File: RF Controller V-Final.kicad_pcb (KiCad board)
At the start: 2 copper layers, 36 parts, among them J2 J_OLED, J3 BAT+, J4 BAT-, SW1 EG1218, U1 Teensy4.0, U3 NRF24L01, U5 AP2112K-3.3, U7 Pitch/Roll, U8 TPS542025DDCR, U9 Throttle/Yaw

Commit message: Board outline
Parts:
- added C2: 47uF, 865080543009:WCAP-ASLI_6.3X5.5_DXL_, F.Cu at (90.8, 108.5)
- C7: value 22u -> 10u
- moved L1 66.1 mm to (56.9, 112.1)
- moved H4 63.0 mm to (115.5, 169.5)
- moved H3 55.9 mm to (127.0, 155.5)
- moved H2 53.5 mm to (112.5, 150.5)
- moved U5 43.5 mm to (56.0, 123.1)
- moved H1 38.2 mm to (117.0, 130.0)
- moved D6 38.2 mm to (89.6, 121.5)
- moved J4 38.2 mm to (91.7, 116.0)
- moved J3 38.2 mm to (87.6, 116.0)
- moved U8 38.0 mm to (56.9, 118.5)
- moved C1 35.2 mm to (67.6, 100.3)
- moved C10 35.2 mm to (67.6, 109.4)
- moved C13 35.2 mm to (67.6, 112.4)
- moved C14 35.2 mm to (67.6, 115.4)
- moved C15 35.2 mm to (67.6, 118.4)
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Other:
- board outline added: 131.9 x 67.5 mm

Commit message: Fixed board measurements
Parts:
- moved H2 172.0 mm to (256.5, 56.5)
- moved H4 150.8 mm to (256.5, 116.0)
- moved H1 75.3 mm to (133.5, 56.5)
- moved H3 40.0 mm to (133.5, 116.0)
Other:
- board size 131.9 x 67.5 mm -> 132 x 67.5 mm
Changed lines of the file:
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@@
 	(footprint "RF_MountingHoles:MountingHole_3.8mm"
 		(layer "F.Cu")
-		(at 112.5 150.5)
+		(at 256.5 56.5)
 		(descr "Non-plated mounting hole, 3.8 mm drill; replaces original Edge.Cuts circle")
 		(tags "mounting hole NPTH 3.8mm")
@@
 	(footprint "RF_MountingHoles:MountingHole_3.8mm"
 		(layer "F.Cu")
-		(at 117 130)
+		(at 133.5 56.5)
 		(descr "Non-plated mounting hole, 3.8 mm drill; replaces original Edge.Cuts circle")
 		(tags "mounting hole NPTH 3.8mm")
@@
 	(footprint "RF_MountingHoles:MountingHole_3.8mm"
 		(layer "F.Cu")
-		(at 115.5 169.5)
+		(at 256.5 116)
 		(descr "Non-plated mounting hole, 3.8 mm drill; replaces original Edge.Cuts circle")
 		(tags "mounting hole NPTH 3.8mm")
@@
 	(footprint "RF_MountingHoles:MountingHole_3.8mm"
 		(layer "F.Cu")
-		(at 127 155.5)
+		(at 133.5 116)
 		(descr "Non-plated mounting hole, 3.8 mm drill; replaces original Edge.Cuts circle")
 		(tags "mounting hole NPTH 3.8mm")
@@
 	)
 	(gr_line
-		(start 132 55.5)
-		(end 132 117)
+		(start 129 55.5)
+		(end 129 117)
 		(stroke
 			(width 0.1)
@@
 	)
 	(gr_arc
-		(start 132 55.5)
-		(mid 132.87868 53.37868)
-		(end 135 52.5)
+		(start 129 55.5)
+		(mid 129.87868 53.37868)
+		(end 132 52.5)
 		(stroke
 			(width 0.1)
-			(type solid)
+			(type default)
 		)
 		(layer "Edge.Cuts")
 	)
 	(gr_line
-		(start 135 52.5)
-		(end 261 52.5)
+		(start 132 52.5)
+		(end 258 52.5)
 		(stroke
 			(width 0.1)
@@
 	)
 	(gr_arc
-		(start 135 120)
-		(mid 132.878681 119.12132)
-		(end 132 117)
+		(start 132 120)
+		(mid 129.87868 119.12132)
+		(end 129 117)
 		(stroke
 			(width 0.1)
-			(type solid)
+			(type default)
 		)
 		(layer "Edge.Cuts")
 	)
 	(gr_line
-		(start 135 120)
-		(end 260.878678 120)
+		(start 132 120)
+		(end 258 120)
 		(stroke
-			(width 0.05)
-			(type default)
+			(width 0.1)
+			(type solid)
 		)
 		(layer "Edge.Cuts")
 	)
 	(gr_arc
-		(start 261 52.5)
-		(mid 263.044203 53.420281)
-		(end 263.87868 55.5)
+		(start 258 52.5)
+		(mid 260.12132 53.37868)
+		(end 261 55.5)
 		(stroke
 			(width 0.1)
@@
 	)
 	(gr_line
-		(start 263.87868 55.5)
-		(end 263.87868 117)
+		(start 261 55.5)
+		(end 261 117)
 		(stroke
 			(width 0.1)
@@
 	)
 	(gr_arc
-		(start 263.87868 117)
-		(mid 262.999999 119.121321)
-		(end 260.878678 120)
+		(start 261 117)
+		(mid 260.12132 119.12132)
+		(end 258 120)
 		(stroke
 			(width 0.1)
-			(type solid)
+			(type default)
 		)
 		(layer "Edge.Cuts")
 	)
+	(dimension
+		(type orthogonal)
+		(layer "Edge.Cuts")
+		(pts
+			(xy 132 52.5) (xy 258 52.5)
+		)
+		(height -4)
+		(orientation 0)
+		(format
+			(prefix "")
+			(suffix "")
+			(units 3)
+			(units_format 0)
+			(precision 4)
+			(suppress_zeroes yes)
+		)
+		(style
+			(thickness 0.05)
+			(arrow_length 1.27)
+			(text_position_mode 0)
+			(arrow_direction outward)
+			(extension_height 0.58642)
+			(extension_offset 0.5)
+			(keep_text_aligned yes)
+		)
+		(gr_text "126"
+			(at 195 47.35 0)
+			(layer "Edge.Cuts")
+			(effects
+				(font
+					(size 1 1)
+					(thickness 0.15)
+				)
+			)
+		)
+	)
+	(dimension
+		(type orthogonal)
+		(layer "Edge.Cuts")
+		(pts
+			(xy 258 52.5) (xy 258 55.5)
+		)
+		(height 5.5)
+		(orientation 1)
+		(format
+			(prefix "")
+			(suffix "")
+			(units 3)
+			(units_format 0)
+			(precision 4)
+			(suppress_zeroes yes)
+		)
+		(style
+			(thickness 0.05)
+			(arrow_length 1.27)
+			(text_position_mode 0)
+			(arrow_direction outward)
+			(extension_height 0.58642)
+			(extension_offset 0.5)
+			(keep_text_aligned yes)
+		)
+		(gr_text "3"
+			(at 262.35 54 90)
+			(layer "Edge.Cuts")
+			(effects
+				(font
+					(size 1 1)
+					(thickness 0.15)
+				)
+			)
+		)
+	)
+	(dimension
+		(type orthogonal)
+		(layer "Edge.Cuts")
+		(pts
+			(xy 261 55.5) (xy 261 117)
+		)
+		(height 4)
+		(orientation 1)
+		(format
+			(prefix "")
+			(suffix "")
+			(units 3)
+			(units_format 0)
+			(precision 4)
+			(suppress_zeroes yes)
+		)
+		(style
+			(thickness 0.05)
+			(arrow_length 1.27)
+			(text_position_mode 0)
+			(arrow_direction outward)
+			(extension_height 0.58642)
+			(extension_offset 0.5)
+			(keep_text_aligned yes)
+		)
+		(gr_text "61.5"
+			(at 263.85 86.25 90)
+			(layer "Edge.Cuts")
+			(effects
+				(font
+					(size 1 1)
+					(thickness 0.15)
+				)
+			)
+		)
+	)
 	(embedded_fonts no)

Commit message: Placed some components
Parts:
- ?: renamed from U1; value Teensy4.0 -> (none)
- moved U7 183.1 mm to (210.0, 115.5)
- moved J2 160.2 mm to (235.5, 58.3)
- moved U9 150.7 mm to (180.0, 89.5), turned to 180 degrees
- moved U3 138.7 mm to (206.4, 62.0), turned to 90 degrees
- moved ? 121.6 mm to (148.6, 74.0)
- moved D6 95.6 mm to (161.0, 58.0), turned to 180 degrees
- moved C2 91.4 mm to (174.0, 70.5)
- moved SW1 76.1 mm to (148.5, 58.0)

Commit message: Component layout V1
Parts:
- removed ?: , teensy:Teensy40
- added U1: Teensy4.0, teensy:Teensy40, F.Cu at (101.5, 93.5)
- C11: value 22u -> 10u
- C12: value 10u -> 22u
- D7: value APT2012LZGCK -> (none)
- SW1: value EG1218 -> (none)
- U5: value AP2112K-3.3 -> (none)
- U8: value TPS542025DDCR -> (none)
- moved C1 109.6 mm to (175.5, 81.5)
- moved R2 107.6 mm to (175.5, 72.5), turned to 180 degrees
- moved R1 105.9 mm to (175.5, 76.5)
- moved U5 96.2 mm to (138.5, 73.5)
- moved C6 81.0 mm to (145.0, 79.5)
- moved C14 80.4 mm to (139.0, 78.5), turned to 180 degrees
- moved C5 78.7 mm to (145.0, 71.0)
- moved C11 78.6 mm to (145.0, 74.5)
- moved L1 78.3 mm to (125.0, 73.5)
- moved U8 75.5 mm to (116.0, 71.5)
- moved C15 75.5 mm to (131.0, 77.5), turned to 180 degrees
- moved C12 65.5 mm to (132.0, 72.0), turned to 90 degrees
- moved R7 62.1 mm to (119.5, 77.5), turned to 90 degrees
- moved R6 57.5 mm to (115.0, 76.5), turned to 180 degrees
- moved D6 55.4 mm to (107.5, 72.5)
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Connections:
- net Net-(U8-SW) renamed /BUCK_SW
- C11 pad 1: /5V_IN -> /3.3V_OUT
- C12 pad 1: /3.3V_OUT -> /5V_IN
- SW1 pad 1: unconnected-(SW1-A-Pad1) -> /VBAT
- SW1 pad 3: /VBAT -> unconnected-(SW1-C-Pad3)

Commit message: PCB Wiring V1
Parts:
- turned R3 to 180 degrees
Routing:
- net /3.3V_OUT: track 0.00 -> 151.6 mm
- net GND: track 0.00 -> 98.5 mm, vias 0 -> 19
- net /9V_IN: track 0.00 -> 23.7 mm, vias 0 -> 5
- net Net-(U8-BOOT): track 0.00 -> 15.9 mm
- net /ADC7: track 0.00 -> 14.7 mm
- net /SW_OUT: track 0.00 -> 14.2 mm
- net Net-(U8-EN): track 0.00 -> 10.3 mm, vias 0 -> 4
- net /VBAT: track 0.00 -> 8.74 mm
- net /BUCK_SW: track 0.00 -> 8.61 mm
- net /ADC6: track 0.00 -> 7.66 mm, vias 0 -> 4
- net Net-(D7-A): track 0.00 -> 3.18 mm
- added copper zone on F.Cu, net /5V_IN
- added copper zone on B.Cu, net GND

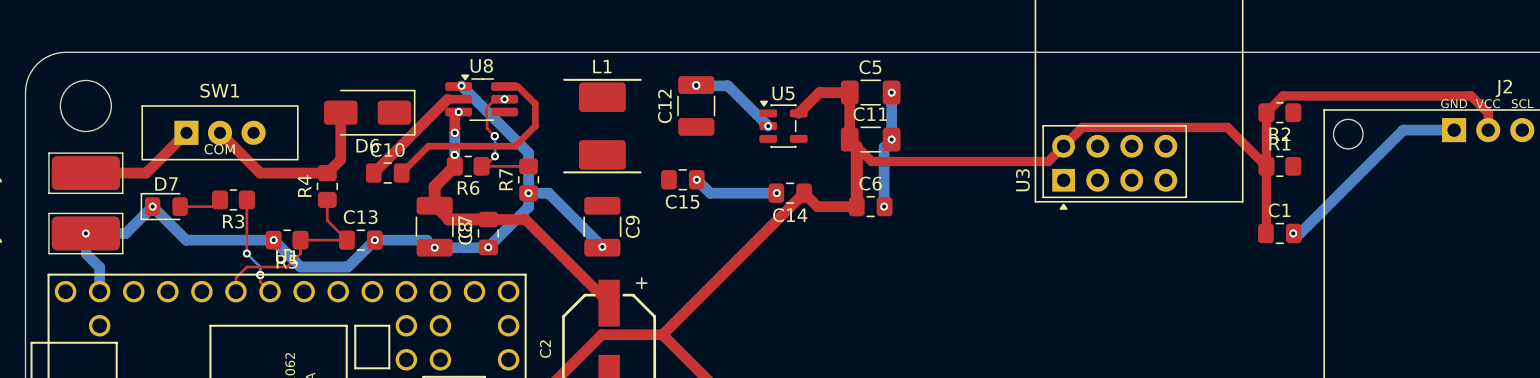
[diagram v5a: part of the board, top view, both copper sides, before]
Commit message: Replaced ground wires with vias at nodes
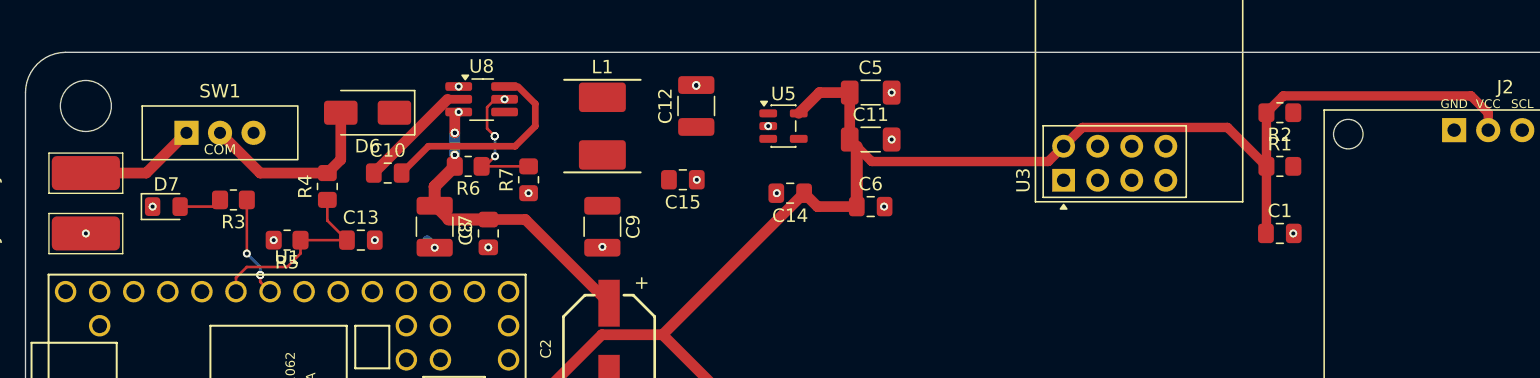
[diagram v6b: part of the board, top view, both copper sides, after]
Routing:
- net GND: track 98.5 -> 1.34 mm, vias 19 -> 18
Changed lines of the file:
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@@
-	)
-	(via
-		(at 87.53 85.84)
-		(size 0.6)
-		(drill 0.3)
-		(layers "F.Cu" "B.Cu")
-		(net "GND")
 	)
 	(via
@@
 	)
 	(via
+		(at 114.29 70.55)
+		(size 0.6)
+		(drill 0.3)
+		(layers "F.Cu" "B.Cu")
+		(net "GND")
+	)
+	(via
 		(at 116.5 82.5375)
 		(size 0.6)
@@
 	(via
 		(at 91.475 79.5)
-		(size 0.6)
-		(drill 0.3)
-		(layers "F.Cu" "B.Cu")
-		(net "GND")
-	)
-	(via
-		(at 114.5 70.5)
 		(size 0.6)
 		(drill 0.3)
@@
 	)
 	(segment
-		(start 86.5 81.5)
-		(end 86.5 83)
-		(width 0.7)
-		(layer "B.Cu")
-		(net "GND")
-	)
-	(segment
-		(start 132 70.5)
-		(end 134.3625 70.5)
-		(width 0.8)
-		(layer "B.Cu")
-		(net "GND")
-	)
-	(segment
-		(start 133.0375 78.5)
-		(end 132.0375 77.5)
-		(width 0.8)
-		(layer "B.Cu")
-		(net "GND")
-	)
-	(segment
-		(start 146.5625 74.5)
-		(end 146.5625 71)
-		(width 0.8)
-		(layer "B.Cu")
-		(net "GND")
-	)
-	(segment
-		(start 106.0375 84)
-		(end 108.0375 82)
-		(width 0.8)
-		(layer "B.Cu")
-		(net "GND")
-	)
-	(segment
-		(start 184.7 73.8)
-		(end 188.49 73.8)
-		(width 0.8)
-		(layer "B.Cu")
-		(net "GND")
-	)
-	(segment
-		(start 121 78.5)
-		(end 119.5 78.5)
-		(width 0.8)
-		(layer "B.Cu")
-		(net "GND")
-	)
-	(segment
-		(start 134.3625 70.5)
-		(end 137.3625 73.5)
-		(width 0.8)
-		(layer "B.Cu")
-		(net "GND")
-	)
-	(segment
-		(start 146 75.0625)
-		(end 146.5625 74.5)
-		(width 0.7)
-		(layer "B.Cu")
-		(net "GND")
-	)
-	(segment
-		(start 86.5 81.5)
-		(end 89.475 81.5)
-		(width 0.8)
-		(layer "B.Cu")
-		(net "GND")
-	)
-	(segment
-		(start 100.5 82)
-		(end 102.5 84)
-		(width 0.8)
-		(layer "B.Cu")
-		(net "GND")
-	)
-	(segment
-		(start 86.5 83)
-		(end 87.53 84.03)
-		(width 0.8)
-		(layer "B.Cu")
-		(net "GND")
-	)
-	(segment
-		(start 146 79.5)
-		(end 146 75.0625)
-		(width 0.8)
-		(layer "B.Cu")
-		(net "GND")
-	)
-	(segment
-		(start 87.53 84.03)
-		(end 87.53 85.84)
-		(width 0.8)
-		(layer "B.Cu")
-		(net "GND")
-	)
-	(segment
-		(start 102.5 84)
-		(end 106.0375 84)
-		(width 0.8)
-		(layer "B.Cu")
-		(net "GND")
-	)
-	(segment
-		(start 119.5 75.5)
-		(end 119.5 78.5)
-		(width 0.8)
-		(layer "B.Cu")
-		(net "GND")
-	)
-	(segment
-		(start 119.5 79.5375)
-		(end 116.475 82.5625)
-		(width 0.8)
-		(layer "B.Cu")
-		(net "GND")
-	)
-	(segment
-		(start 138 78.5)
-		(end 133.0375 78.5)
-		(width 0.8)
-		(layer "B.Cu")
-		(net "GND")
-	)
-	(segment
-		(start 177 81.5)
-		(end 184.7 73.8)
-		(width 0.8)
-		(layer "B.Cu")
-		(net "GND")
-	)
-	(segment
-		(start 89.475 81.5)
-		(end 91.475 79.5)
-		(width 0.8)
-		(layer "B.Cu")
-		(net "GND")
-	)
-	(segment
-		(start 112.5 82.5625)
-		(end 116.475 82.5625)
-		(width 0.8)
-		(layer "B.Cu")
-		(net "GND")
-	)
-	(segment
 		(start 111.9375 82)
 		(end 112.5 82.5625)
@@
 		(layer "B.Cu")
 		(net "GND")
-	)
-	(segment
-		(start 176.5 81.5)
-		(end 177 81.5)
-		(width 0.8)
-		(layer "B.Cu")
-		(net "GND")
-	)
-	(segment
-		(start 91.475 79.5)
-		(end 93.975 82)
-		(width 0.8)
-		(layer "B.Cu")
-		(net "GND")
-	)
-	(segment
-		(start 119.5 78.5)
-		(end 119.5 79.5375)
-		(width 0.8)
-		(layer "B.Cu")
-		(net "GND")
-	)
-	(segment
-		(start 114.5 70.5)
-		(end 119.5 75.5)
-		(width 0.8)
-		(layer "B.Cu")
-		(net "GND")
-	)
-	(segment
-		(start 93.975 82)
-		(end 100.5 82)
-		(width 0.8)
-		(layer "B.Cu")
-		(net "GND")
-	)
-	(segment
-		(start 108.0375 82)
-		(end 111.9375 82)
-		(width 0.8)
-		(layer "B.Cu")
-		(net "GND")
-	)
-	(segment
-		(start 125 82.5)
-		(end 121 78.5)
-		(width 0.8)
-		(layer "B.Cu")
-		(net "GND")

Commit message: Board 5V and GND UPD
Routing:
- net /CSN: track 0.00 -> 62.1 mm, vias 0 -> 1
- net /MOSI: track 0.00 -> 62.0 mm, vias 0 -> 4
- net /MISO: track 0.00 -> 58.7 mm, vias 0 -> 2
- net /D10: track 0.00 -> 52.3 mm
- net /SCK: track 0.00 -> 49.9 mm, vias 0 -> 3
- net /SDA: track 0.00 -> 24.2 mm, vias 0 -> 3
- net /SCL: track 0.00 -> 23.7 mm, vias 0 -> 4
- net Net-(U8-EN): track 10.3 -> 12.2 mm

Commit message: Wiring complete, errors need fixing
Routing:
- net /SDA: track 24.2 -> 107.6 mm, vias 3 -> 8
- net /SCL: track 23.7 -> 103.6 mm, vias 4 -> 16
- net /ADC2: track 0.00 -> 77.9 mm, vias 0 -> 3
- net /ADC3: track 0.00 -> 65.9 mm
- net /CE: track 0.00 -> 61.4 mm, vias 0 -> 4
- net /ADC1: track 0.00 -> 59.9 mm
- net /ADC0: track 0.00 -> 59.1 mm
- net /D9: track 0.00 -> 47.0 mm, vias 0 -> 3
